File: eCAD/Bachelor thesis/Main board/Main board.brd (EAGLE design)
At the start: 160 x 100 mm, 111 parts, among them IC1 ESP32-WROOM-32E_M113EH3200PH3Q, IC10 SMS3.3.TCT, IC2 BC660K-GL, IC3 SMS3.3.TCT, IC4 AP9101CK6-ADTRG1, IC5 FDS6898A, IC6 MCP73871-2CCI_ML, IC7 ME6211C33M5G-N, IC8 ME6211C33M5G-N, IC9 SMS3.3.TCT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

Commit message: component placement
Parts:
- JP1: value (none) -> ESP_RST
- JP2: value (none) -> ESP_BOOT
- JP3: value (none) -> NB_RST
- JP4: value (none) -> NB_BOOT
- JP5: value (none) -> PSM_EINT
- R9: device rcl:R1206 -> rcl:R0805
- moved J6 231.9 mm to (115.8, -2.20)
- moved IC9 230.2 mm to (79.0, 3.10)
- moved IC10 218.9 mm to (83.5, 3.11)
- moved D1 200.9 mm to (35.4, 18.0), turned to 0 degrees
- moved D4 197.5 mm to (19.7, 15.1)
- moved J4 197.0 mm to (51.8, 12.8)
- moved J5 197.0 mm to (67.8, 12.8)
- moved J3 196.2 mm to (32.8, 7.20)
- moved D2 195.1 mm to (20.0, 10.8)
- moved R11 195.1 mm to (10.8, 10.8)
- moved R12 195.1 mm to (13.0, 10.8)
- moved $3_29_$_2023-03-21_17-43-41 195.1 mm to (16.5, 4.52)
- moved R13 195.1 mm to (15.2, 10.8)
- moved C1 194.0 mm to (84.6, 98.4), turned to 90 degrees
- moved SJ4 193.2 mm to (17.5, 15.1)
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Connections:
- net ESP_FLASH renamed ESP_BOOT
- new net ESP_ENABLE: C1.1, JP1.2, R1.1
- net ESP_EN: no longer C1.1, JP1.2, R1.1
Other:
- board size 160 x 100 mm -> 84 x 100 mm

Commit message: Routing
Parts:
- C1, C10, C11, C12, C13, C15, C16, C17, C18, C19, C20, C21, C22, C23, C24, C25, C3, C4, C5, C6, C7, C8, C9: device rcl:C0805 -> rcl:C0603
- D1, D2, D5: value SMBJ6.5A -> PTVS6V5S1UR,115; device 1-component-search:DIOM5436X261N -> 1-component-search:SOD123W
- JP10: device jumper:JP2 -> jumper:JP1
- R1, R11, R12, R13, R14, R17, R18, R19, R2, R20, R21, R22, R23, R3, R4, R5, R6, R7, R8, R9: device rcl:R0805 -> rcl:R0603
- moved JP7 50.4 mm to (84.5, 59.2), turned to 0 degrees
- moved C1 48.3 mm to (88.2, 50.2), turned to 0 degrees
- moved R1 45.8 mm to (88.2, 52.4), turned to 0 degrees
- moved JP2 43.0 mm to (79.4, 51.4), turned to 0 degrees
- moved JP1 42.8 mm to (84.6, 51.4), turned to 0 degrees
- moved R2 42.1 mm to (79.6, 55.2)
- moved C28 36.9 mm to (41.6, 28.6), flipped to the bottom, turned to 180 degrees
- moved J6 33.5 mm to (85.8, 12.8)
- moved HM1 33.1 mm to (42.6, 30.6), flipped to the bottom, turned to 90 degrees
- moved R14 32.1 mm to (78.4, 41.2), flipped to the bottom, turned to 0 degrees
- moved C18 29.7 mm to (78.4, 39.0), flipped to the bottom, turned to 180 degrees
- moved R34 28.5 mm to (66.4, 29.2), flipped to the bottom, turned to 180 degrees
- moved C29 28.4 mm to (66.4, 27.0), flipped to the bottom, turned to 0 degrees
- moved C27 28.3 mm to (41.6, 34.8), flipped to the bottom, turned to 0 degrees
- moved IC4 26.3 mm to (78.2, 35.6), flipped to the bottom, turned to 90 degrees
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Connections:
- removed net ESP_EN: IC1.3
- removed net VCC: IC6.4
- net ESP_ENABLE: now also IC1.3
- net GND: no longer JP10.1
- net N$6: now also JP10.1; no longer JP10.2
- net VIN: now also IC6.4, JP10.2; no longer JP10.3
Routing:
- net I2C_SCL: track 0.00 -> 168.7 mm, vias 0 -> 4
- net I2C_SDA: track 0.00 -> 143.6 mm, vias 0 -> 5
- net VIN: track 0.00 -> 143.5 mm, vias 0 -> 4
- net RAIN_GAUGE_INPUT: track 0.00 -> 130.1 mm, vias 0 -> 3
- net BAT_Q: track 0.00 -> 114.4 mm, vias 0 -> 4
- net VBAT: track 0.00 -> 101.2 mm, vias 0 -> 2
- net DS18B_SIG: track 0.00 -> 89.5 mm, vias 0 -> 5
- net SENS_VDD33: track 0.00 -> 89.3 mm, vias 0 -> 2
- net PSM_EINT: track 0.00 -> 78.6 mm, vias 0 -> 3
- net STAT1: track 0.00 -> 73.3 mm, vias 0 -> 2
- net !PG: track 0.00 -> 73.0 mm, vias 0 -> 2
- net USIM_GND: track 0.00 -> 72.9 mm
- net STAT2: track 0.00 -> 70.9 mm, vias 0 -> 2
- net RESET_QUECTEL: track 0.00 -> 67.8 mm, vias 0 -> 2
- net VOL_SENS: track 0.00 -> 67.8 mm, vias 0 -> 3
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- added copper zone on layer 1, net GND
- added copper zone on layer 15, net GND
- added copper zone on layer 16, net GND
- added copper zone on layer 2, net N$86
- added copper zone on layer 2, net VDD33
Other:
- board size 84 x 100 mm -> 100.2 x 98 mm

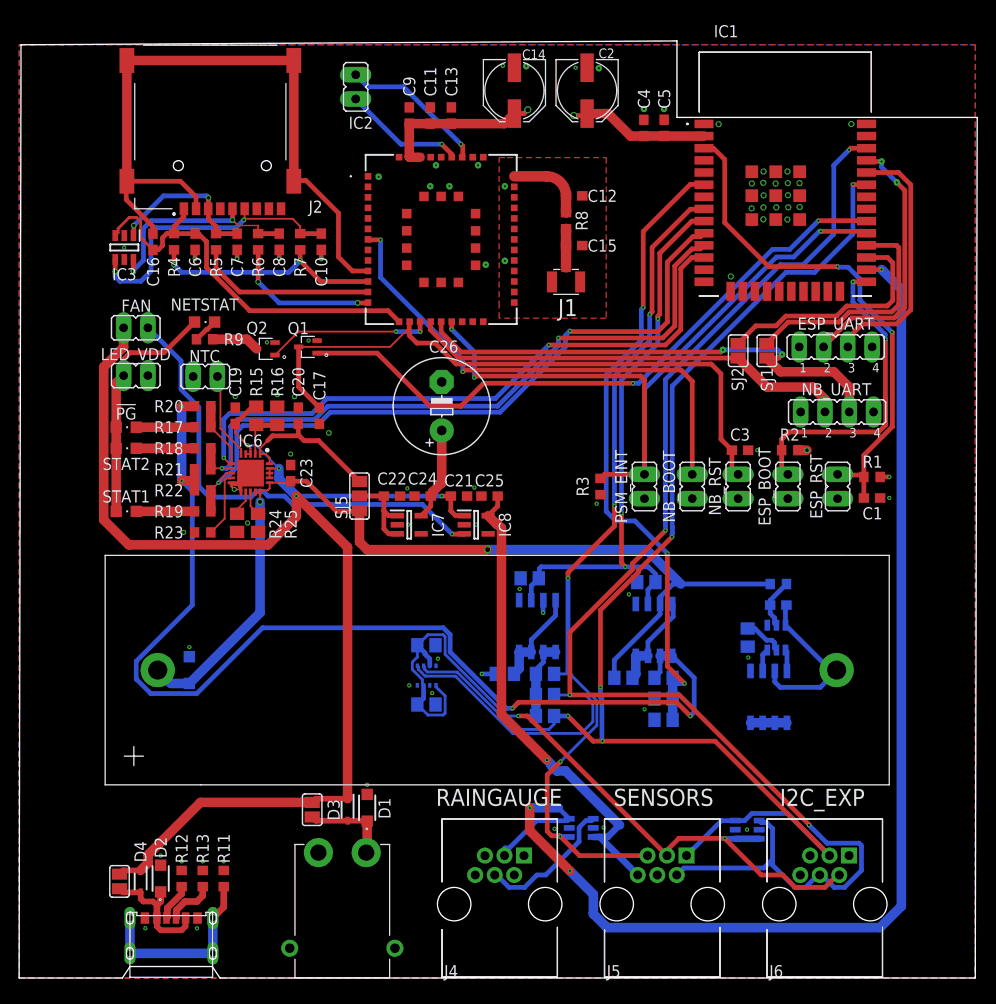
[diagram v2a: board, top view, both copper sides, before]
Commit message: v2 board out in production
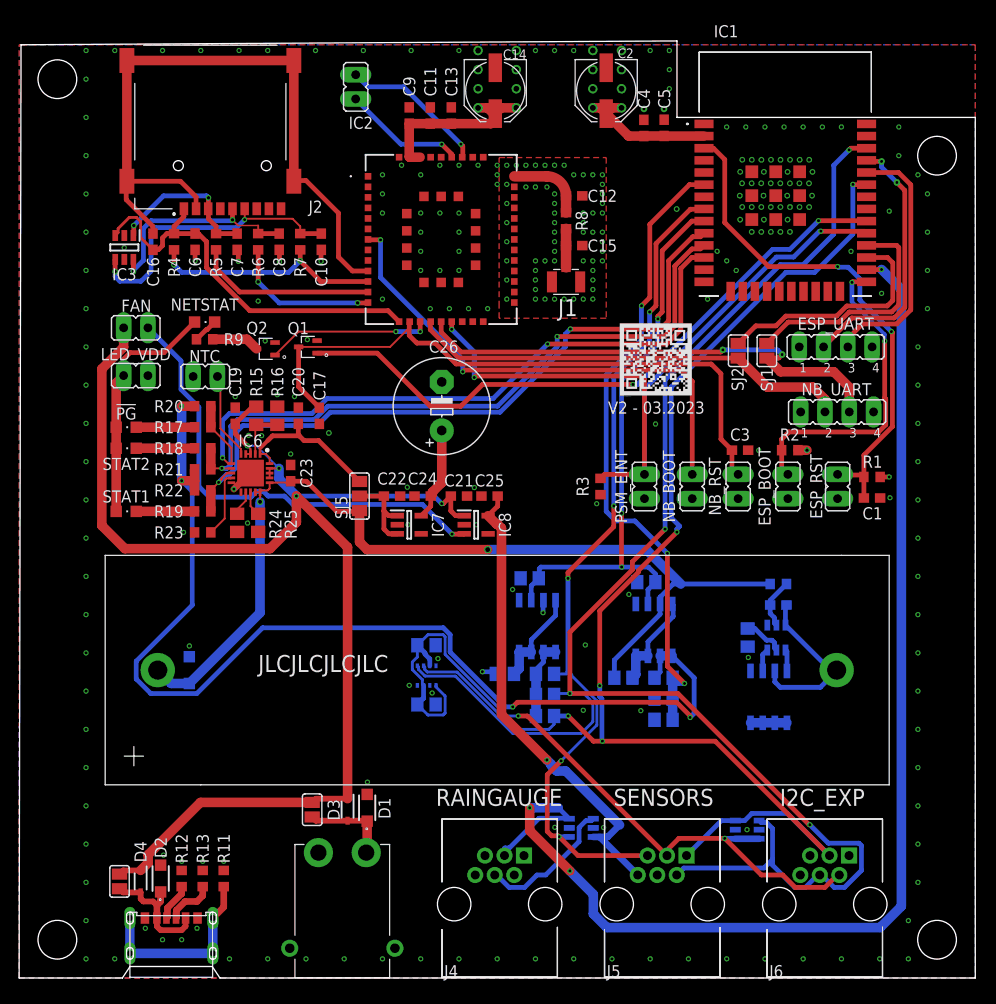
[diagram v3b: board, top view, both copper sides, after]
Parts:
- C26: value 50 -> 30F
- R1, R2, R3: value 10K -> 10k
- R15: value (none) -> 100k
- R16: value (none) -> 330k
- moved C14 2.00 mm to (48.8, 92.8)
- moved C2 2.00 mm to (60.4, 92.8)
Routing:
- net GND: track 15.9 -> 7.33 mm, vias 70 -> 286
- net VIN: track 143.5 -> 145.5 mm
- net VDD33: track 61.9 -> 62.9 mm, vias 6 -> 8
- net I2C_SDA: track 143.6 -> 144.4 mm
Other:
- board size 100.2 x 98 mm -> 100 x 98 mm
- board text added: "C:/Users/jirka/Downloads/bitmap.bmp"
- board text added: "JLCJLCJLCJLC"
- board text added: "V2 - 03.2023"
